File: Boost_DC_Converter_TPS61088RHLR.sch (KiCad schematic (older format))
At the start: 1 part, among them U1 TPS61088RHLR

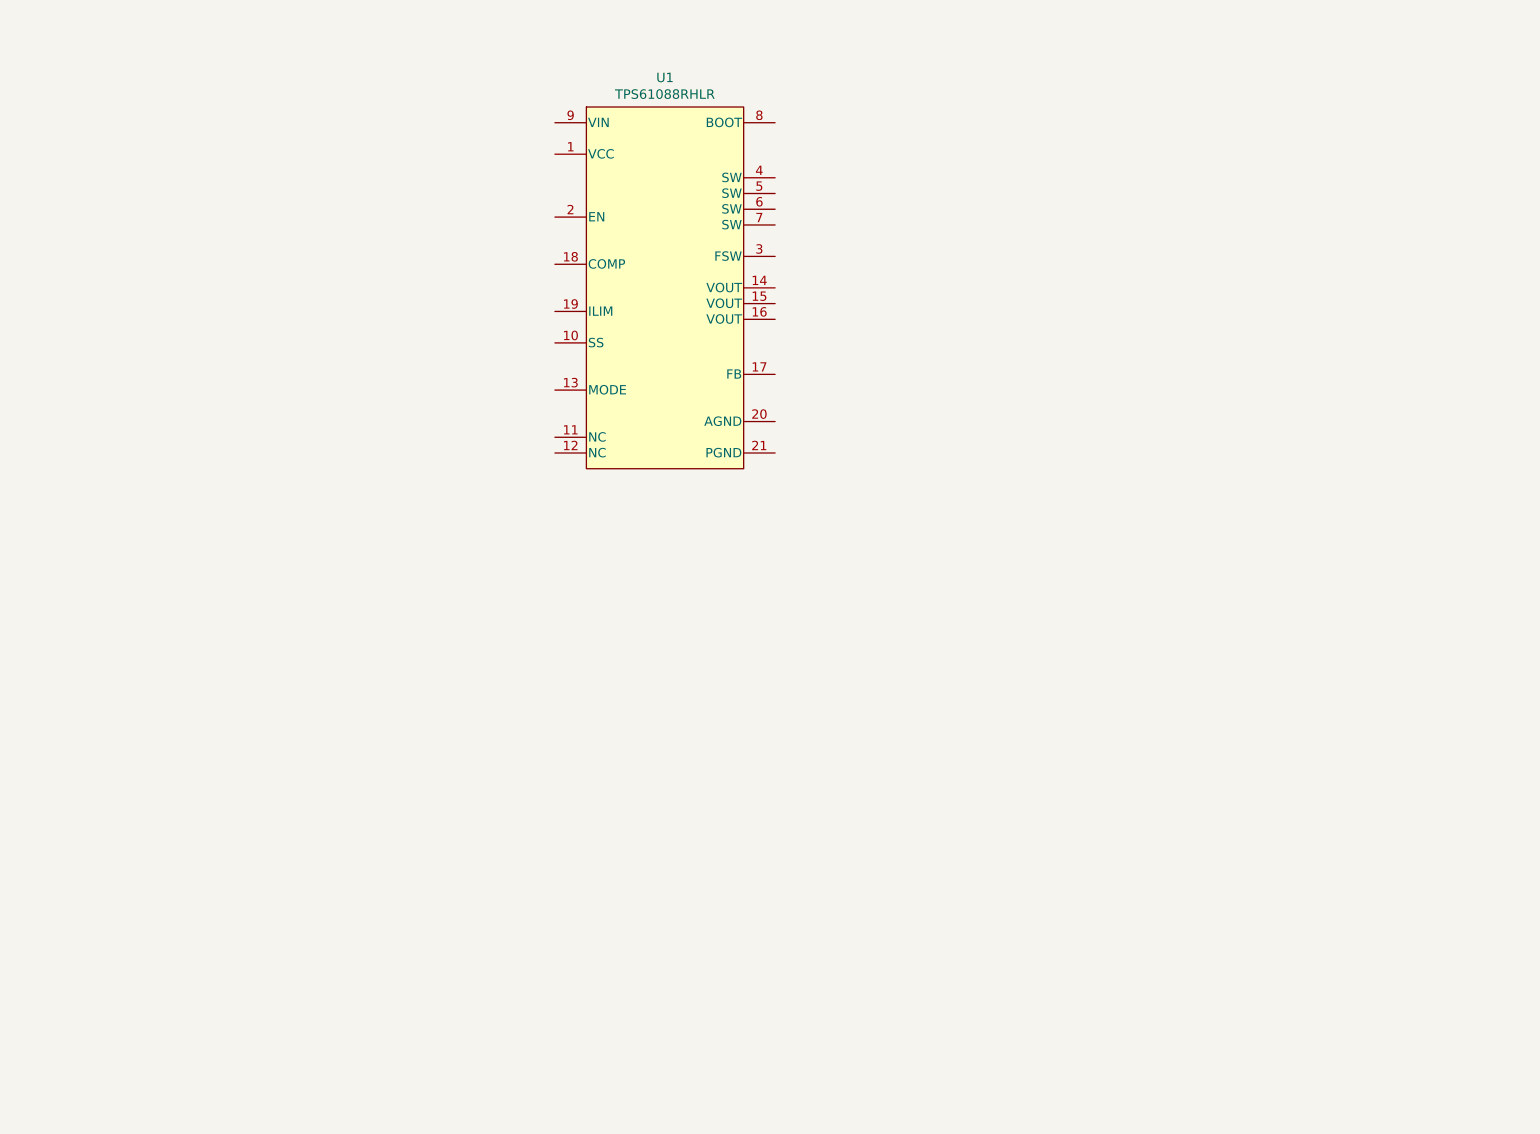
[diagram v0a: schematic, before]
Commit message: Schematic done
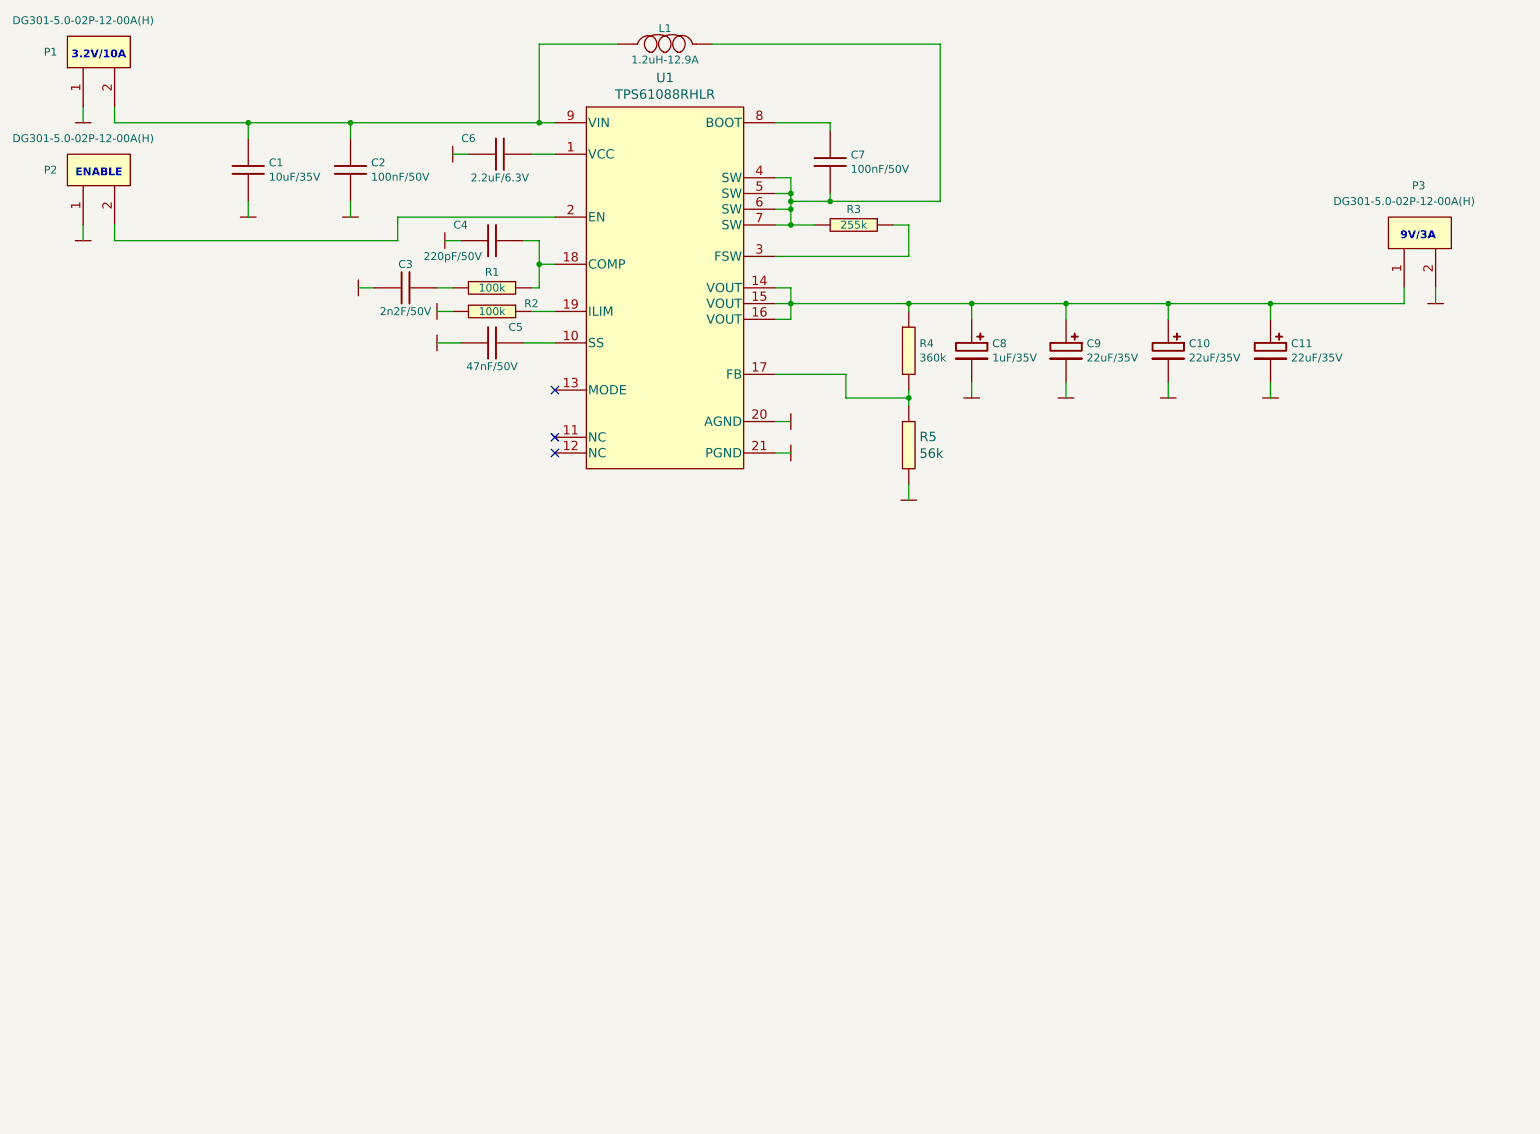
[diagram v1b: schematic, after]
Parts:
- added C1: 10uF/35V, Capacitors_Smd_1210:10uF_35V_X7R_1210, symbol Capacitors_Smd1210:10uF_35V_X7R_1210
- added C10, C11, C9: 22uF/35V, Smd_Tantal:22uF_35V_Size_D, symbol Capacitors_Smd_Tantal:22uF35V
- added C2, C7: 100nF/50V, Capacitors_Smd_0603:100nF_0603, symbol Capacitors_Smd0603:100nF_0603
- added C3: 2n2F/50V, Capacitors_Smd_0603:2.2nF_0603, symbol Capacitors_Smd0603:2n2F_0603
- added C4: 220pF/50V, Capacitors_Smd_0603:220pF_0603, symbol Capacitors_Smd0603:220pF_0603
- added C5: 47nF/50V, Capacitors_Smd_0603:47nF_0603, symbol Capacitors_Smd0603:47nF_0603
- added C6: 2.2uF/6.3V, Capacitors_Smd_0603:2_2uF_0603, symbol Capacitors_Smd0603:2_2uF_0603
- added C8: 1uF/35V, Smd_Tantal:1uF_35V_B_Tantal, symbol Capacitors_Smd_Tantal:1uF_35V_SMD_Tantal
- added L1: 1.2uH-12.9A, Inductors:CDMC8D28NP-1R2MC, symbol Inductors:1.2uH-12.9A
- added P1, P2, P3: DG301-5.0-02P-12-00A(H), Discrete_Connectors:DG301-5.0-02P-12-00A(H), symbol Discrete_Connectors:DG301-5.0-02P-12-00A(H)
- added R1, R2: 100k, Resistor_Smd_0603:100k_0603, symbol Resistors_Smd0603:100k_0603
- added R3: 255k, Resistor_Smd_0603:255k_0603, symbol Resistors_Smd0603:255k
- added R4: 360k, Resistor_Smd_0603:360k_0603, symbol Resistors_Smd0603:360k_0603
- added R5: 56k, Resistor_Smd_0603:56k_0603, symbol Resistors_Smd0603:56k_0603
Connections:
- net at U1.1 (VCC): now also C6.1
- net at U1.10 (SS): now also C5.1
- net at U1.14 (VOUT): now also U1.15 (VOUT), U1.16 (VOUT), C10.1, C11.1, C8.1, C9.1, P3.1, R4.1
- net at U1.17 (FB): now also R4.2, R5.1
- net at U1.18 (COMP): now also C4.1, R1.1
- net at U1.19 (ILIM): now also R2.1
- net at U1.2 (EN): now also P2.2
- net GND: now reaches U1.20 (AGND)
- net GND: now also U1.21 (PGND), C1.2, C10.2, C11.2, C2.2, C3.2, C4.2, C5.2, C6.2, C8.2, C9.2, P1.1, P2.1, P3.2, R2.2, R5.2
- net at U1.3 (FSW): now also R3.1
- net at U1.4 (SW): now also U1.5 (SW), U1.6 (SW), U1.7 (SW), C7.2, L1.2, R3.2
- net at U1.8 (BOOT): now also C7.1
- net at U1.9 (VIN): now also C1.1, C2.1, L1.1, P1.2
- new net: C3.1, R1.2
- no-connect marks 0 -> 3
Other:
- note added: "3.2V/10A"
- note added: "9V/3A"
- note added: "ENABLE"

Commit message: PCB almost done
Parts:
- added MH1, MH2, MH3, MH4: Mounting_Hole_M3_Grounded, Mounting_Holes:Mounting_Hole_M3_Grounded, symbol Mounting_Holes:Mounting_Hole_M3_Grounded
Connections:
- net GND: now also MH1.1, MH2.1, MH3.1, MH4.1
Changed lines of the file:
@@
 Text Notes 4175 4250 0    50   ~ 10
 3.2V/10A
+$Comp
+L Mounting_Holes:Mounting_Hole_M3_Grounded MH4
+U 1 1 5FC178DA
+P 10500 10700
+F 0 "MH4" H 10628 10688 50  0000 L CNN
+F 1 "Mounting_Hole_M3_Grounded" H 10628 10597 50  0000 L CNN
+F 2 "Mounting_Holes:Mounting_Hole_M3_Grounded" H 10550 10500 50  0001 C CNN
+F 3 "" H 10550 10500 50  0001 C CNN
+	1    10500 10700
+	1    0    0    -1
+$EndComp
+$Comp
+L power:GND #PWR0118
+U 1 1 5FC17D0B
+P 10500 11000
+F 0 "#PWR0118" H 10500 11100 30  0001 C CNN
+F 1 "GND" H 10500 10900 30  0001 C CNN
+F 2 "" H 10500 11000 60  0000 C CNN
+F 3 "" H 10500 11000 60  0000 C CNN
+	1    10500 11000
+	1    0    0    -1
+$EndComp
+Wire Wire Line
+	10500 10900 10500 11000
+$Comp
+L Mounting_Holes:Mounting_Hole_M3_Grounded MH3
+U 1 1 5FC1A89E
+P 10500 10200
+F 0 "MH3" H 10628 10188 50  0000 L CNN
+F 1 "Mounting_Hole_M3_Grounded" H 10628 10097 50  0000 L CNN
+F 2 "Mounting_Holes:Mounting_Hole_M3_Grounded" H 10550 10000 50  0001 C CNN
+F 3 "" H 10550 10000 50  0001 C CNN
+	1    10500 10200
+	1    0    0    -1
+$EndComp
+$Comp
+L power:GND #PWR0119
+U 1 1 5FC1AB60
+P 10500 10500
+F 0 "#PWR0119" H 10500 10600 30  0001 C CNN
+F 1 "GND" H 10500 10400 30  0001 C CNN
+F 2 "" H 10500 10500 60  0000 C CNN
+F 3 "" H 10500 10500 60  0000 C CNN
+	1    10500 10500
+	1    0    0    -1
+$EndComp
+Wire Wire Line
+	10500 10400 10500 10500
+$Comp
+L Mounting_Holes:Mounting_Hole_M3_Grounded MH2
+U 1 1 5FC1D214
+P 9100 10700
+F 0 "MH2" H 9228 10688 50  0000 L CNN
+F 1 "Mounting_Hole_M3_Grounded" H 9228 10597 50  0000 L CNN
+F 2 "Mounting_Holes:Mounting_Hole_M3_Grounded" H 9150 10500 50  0001 C CNN
+F 3 "" H 9150 10500 50  0001 C CNN
+	1    9100 10700
+	1    0    0    -1
+$EndComp
+$Comp
+L power:GND #PWR0120
+U 1 1 5FC1D4F2
+P 9100 11000
+F 0 "#PWR0120" H 9100 11100 30  0001 C CNN
+F 1 "GND" H 9100 10900 30  0001 C CNN
+F 2 "" H 9100 11000 60  0000 C CNN
+F 3 "" H 9100 11000 60  0000 C CNN
+	1    9100 11000
+	1    0    0    -1
+$EndComp
+Wire Wire Line
+	9100 10900 9100 11000
+$Comp
+L Mounting_Holes:Mounting_Hole_M3_Grounded MH1
+U 1 1 5FC1D4FD
+P 9100 10200
+F 0 "MH1" H 9228 10188 50  0000 L CNN
+F 1 "Mounting_Hole_M3_Grounded" H 9228 10097 50  0000 L CNN
+F 2 "Mounting_Holes:Mounting_Hole_M3_Grounded" H 9150 10000 50  0001 C CNN
+F 3 "" H 9150 10000 50  0001 C CNN
+	1    9100 10200
+	1    0    0    -1
+$EndComp
+$Comp
+L power:GND #PWR0121
+U 1 1 5FC1D507
+P 9100 10500
+F 0 "#PWR0121" H 9100 10600 30  0001 C CNN
+F 1 "GND" H 9100 10400 30  0001 C CNN
+F 2 "" H 9100 10500 60  0000 C CNN
+F 3 "" H 9100 10500 60  0000 C CNN
+	1    9100 10500
+	1    0    0    -1
+$EndComp
+Wire Wire Line
+	9100 10400 9100 10500
 $EndSCHEMATC
